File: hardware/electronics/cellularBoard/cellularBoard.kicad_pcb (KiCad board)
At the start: 4 copper layers, 22 x 36.8 mm, 56 parts, among them J1 Standoff, J2 M.2_E_Key_PCB_Edge, Q1 DMG1013TQ-7, U1 AP7361E, U2 TXS0104VxRUTR, U3 ZED-F9P, U4 OPA344

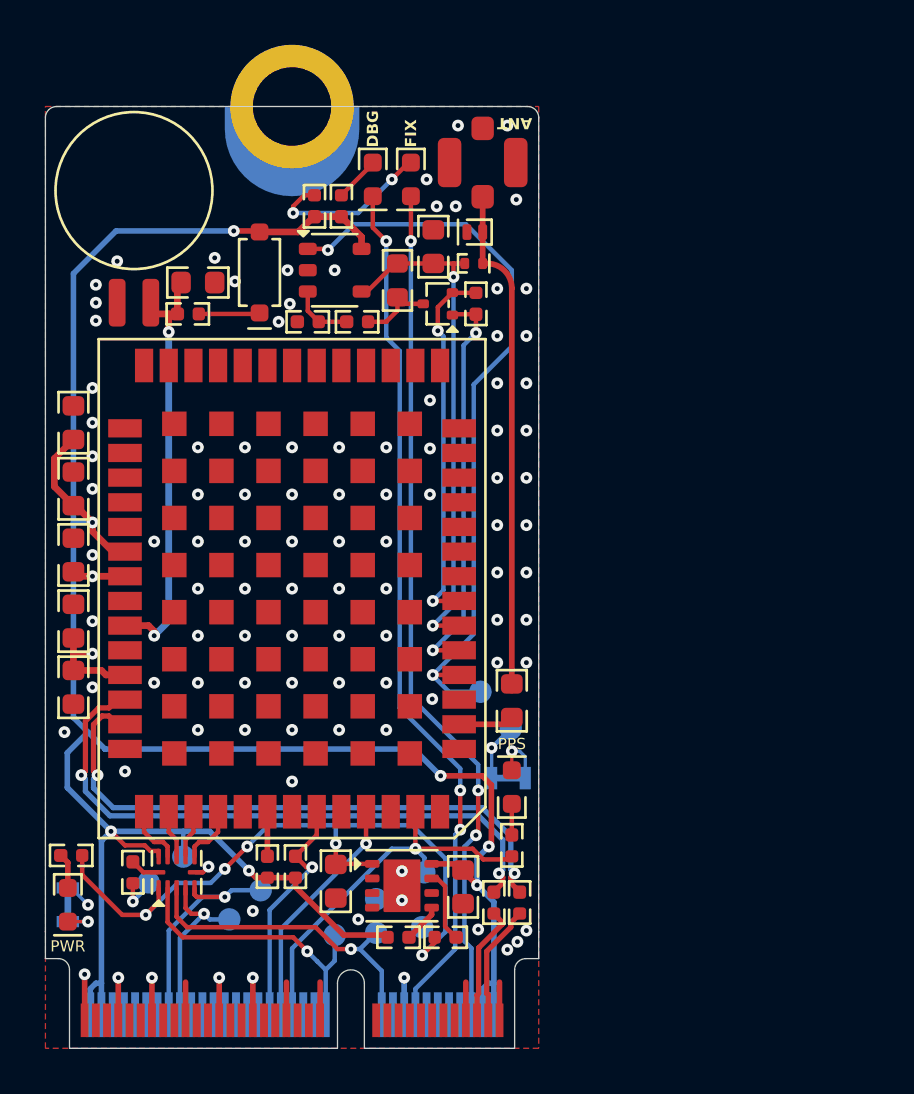
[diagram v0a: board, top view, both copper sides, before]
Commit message: first attempt for layout and routing
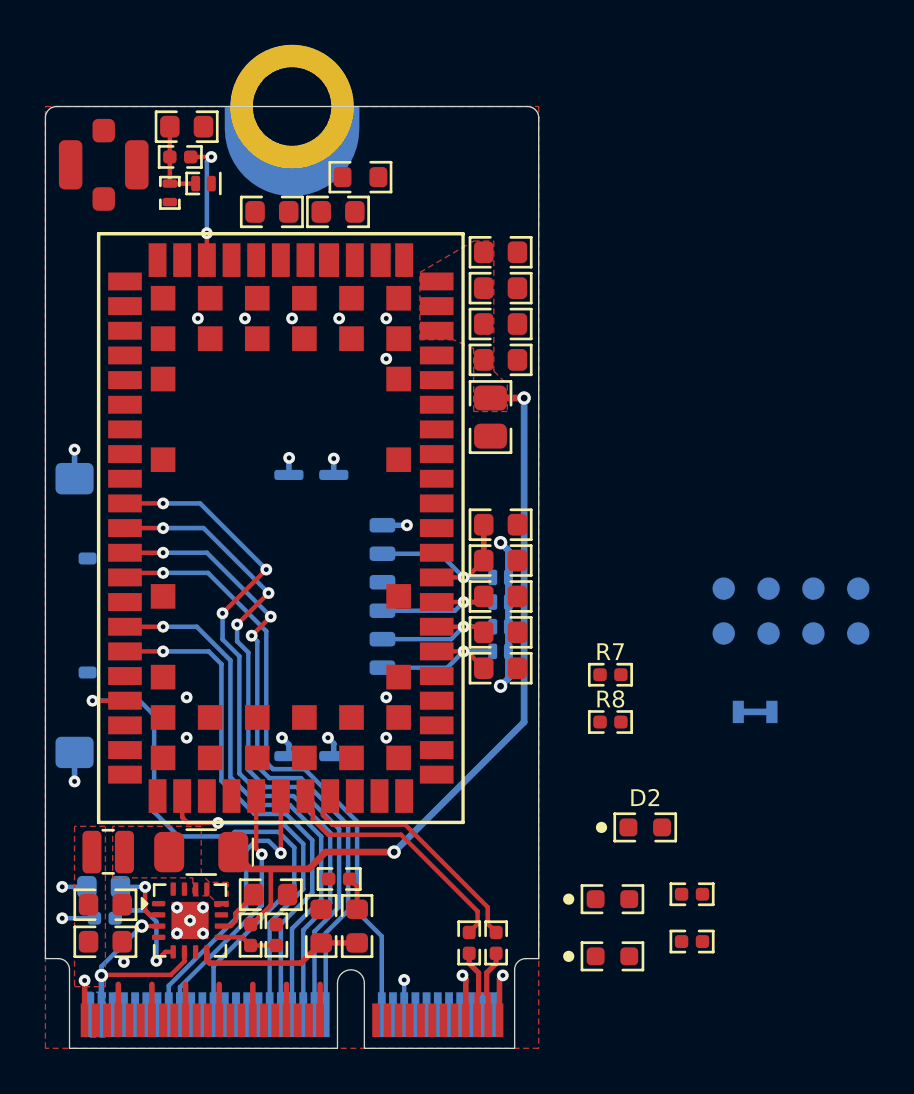
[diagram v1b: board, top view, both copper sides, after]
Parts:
- removed BT1: ~, lib_fp:MS621FE-FL11E
- removed JP2: ~, lib_fp:Jumper_2_Bridged
- removed Q1: DMG1013TQ-7, lib_fp:SOT23-3P50_160X160X75L22X22N
- removed R12: 27R, lib_fp:CRCW0402
- removed R13, R14: 10K, lib_fp:CRCW0402
- removed R15: 1K, lib_fp:CRCW0402
- removed R16: 100K, lib_fp:CRCW0402
- removed REF**: OSHW-Logo2_7.3x6mm_SilkScreen, DS-Logos-and-Graphics:OSHW-Logo2_7.3x6mm_SilkScreen
- removed TP10, TP11, TP9: ~, lib_fp:TP_1mm
- removed U3: ZED-F9P, lib_fp:ZED-F9P-04B_UBL
- removed U4: OPA344, lib_fp:SOT23-5P95_280X300X110L40X38N
- added C11: 15pF, lib_fp:MLCC0603, F.Cu at (149.3, 86.1)
- added C12: 47pF, lib_fp:MLCC0603, F.Cu at (149.3, 98.2)
- added C13: 100nF, lib_fp:MLCC0603, F.Cu at (149.3, 96.7)
- added C14: 47pF, lib_fp:MLCC0603, F.Cu at (149.3, 99.8)
- added C15: 47pF, lib_fp:MLCC0603, F.Cu at (149.3, 103.0)
- added C16: 47pF, lib_fp:MLCC0603, F.Cu at (149.3, 101.5)
- added C17: 15pF, lib_fp:MLCC0603, F.Cu at (142.1, 82.7)
- added C18: 33pF, lib_fp:MLCC0603, F.Cu at (139.1, 82.7)
- added C19: 27pF, lib_fp:MLCC0603, F.Cu at (135.3, 78.9)
- added D7: TVS, lib_fp:XDFN2P65_100X60X50L50X25L, B.Cu at (149.3, 102.3)
- added D8: TVS, lib_fp:XDFN2P65_100X60X50L50X25L, B.Cu at (149.3, 101.2)
- added D9: TVS, lib_fp:XDFN2P65_100X60X50L50X25L, F.Cu at (136.1, 81.4)
- added J3: 0786463001, lib_fp:786463001, B.Cu at (130.3, 100.7)
- added L2: 39nH, lib_fp:L_0603, F.Cu at (143.1, 81.2)
- added L3: 68nH, lib_fp:L_0402, F.Cu at (134.6, 81.8)
- C10: value 10nF -> 68pF
- C2, C8: value 2.2uF -> 100nF
- C3: moved to B.Cu
- C4: value 100nF -> 10nF
- C5: value 100nF -> 330pF
- C6: value 1uF -> 10nF
- C7: value 100nF -> 22uF; footprint lib_fp:MLCC0603 -> lib_fp:MLCC0805
- C9: value 47pF -> 10nF
- D1: value LTST-C190KYKT -> MBR230S1F; footprint lib_fp:LTST-0603 -> lib_fp:SOD123F
- D2: value LTST-C190KGKT -> LTST-C190KYKT
- D3: value LTST-C190KRKT -> LTST-C190KGKT
- D4: value LTST-C190TBKT -> LTST-C190KRKT
- D5: value B0540WQ -> TVS; footprint lib_fp:SOD123 -> lib_fp:XDFN2P65_100X60X50L50X25L; moved to B.Cu
- D6: value PTVS4V5D1BLYL -> TVS; footprint lib_fp:SOD882 -> lib_fp:XDFN2P65_100X60X50L50X25L; moved to B.Cu
- L1: value 47nH -> 680nH; footprint lib_fp:L_0402 -> lib_fp:L_0806
- R1: value 10K -> 9K31; moved to B.Cu
- R10: value 10R -> 27R; footprint lib_fp:CRCW0603 -> lib_fp:CRCW0402
- R11: value 27R -> 10K
- R2: value 10K -> 301R
- R3: value 1K -> 6K98
- R4: value 4K7 -> 2K49
- R6: value 10K -> 4K7
- R7: value 4K7 -> 10K
- R9: value 3K3 -> 27R
- U1: value AP7361E -> LM51571-Q1; footprint lib_fp:UDFN8P65_300X300X60L25X45L -> lib_fp:RTE0016K
- U2: value TXS0104VxRUTR -> SARA-R520-02B; footprint lib_fp:RUT0012A -> lib_fp:SARA-R52X_UBL
- moved R11 36.5 mm to (135.0, 80.2), turned to 180 degrees
- moved R5 34.4 mm to (157.8, 113.1), turned to 0 degrees
- moved D3 33.8 mm to (154.3, 113.3), turned to 0 degrees
- moved R4 32.5 mm to (139.3, 115.0), turned to 90 degrees
- moved TP1 32.4 mm to (165.2, 99.5)
- moved JP1 31.8 mm to (160.7, 105.0), turned to 180 degrees
- moved R9 31.2 mm to (149.1, 115.3), turned to 90 degrees
- moved L1 30.9 mm to (131.8, 111.2), turned to 0 degrees
- moved D2 30.7 mm to (155.8, 110.2), turned to 0 degrees
- moved R10 29.7 mm to (147.9, 115.3), turned to 90 degrees
- moved TP7 28.8 mm to (159.2, 99.5)
- moved TP5 28.2 mm to (161.2, 99.5)
- moved TP6 25.4 mm to (161.2, 101.5)
- moved TP4 25.2 mm to (163.2, 101.5)
- moved R6 25.1 mm to (157.8, 115.2), turned to 0 degrees
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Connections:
- AE1 pad 1: /Cellular Module/ANT_IN -> Net-(AE1-A)
- C10 pad 1: /Cellular Module/ANT_SHORT_N -> +3V8
- C2 pad 1: +1V8 -> +3V3
- C3 pad 1: +3V3 -> VSS
- C3 pad 2: VSS -> Net-(U1-VCC)
- C4 pad 1: +3V3 -> Net-(U1-SS)
- C5 pad 1: +3V3 -> Net-(U1-COMP)
- C6 pad 1: +3V3 -> Net-(U1-COMP)
- C6 pad 2: VSS -> Net-(C6-Pad2)
- C7 pad 1: +3V3 -> +3V8
- C8 pad 1: VBAT -> +3V8
- C9 pad 1: /Cellular Module/ANT_IN -> +3V8
- C9 pad 2: /Cellular Module/RF_IN -> VSS
- D1 pad 1: Net-(D1-Pad1) -> /SW
- D1 pad 2: Net-(D1-Pad2) -> +3V8
- D2 pad 1: Net-(D2-Pad1) -> +3V8
- D2 pad 2: Net-(J2-~{LED_1}) -> Net-(D2-Pad2)
- D3 pad 2: Net-(J2-~{LED_2}) -> Net-(J2-~{LED_1})
- D4 pad 2: Net-(D4-Pad2) -> Net-(J2-~{LED_2})
- D5 pad 1: +3V3 -> VSS
- D5 pad 2: Net-(D5-Pad2) -> VSIM
- D6 pad 2: /Cellular Module/ANT_IN -> /Cellular Modem/SIM_RST
- J2 pad 22: /ZED_RXD_1V8 -> /SARA_RXD_1V8
- J2 pad 32: /ZED_TXD_1V8 -> /SARA_TXD_1V8
- J2 pad 34: unconnected-(J2-UART_CTS-Pad34) -> /SARA_CTS_1V8
- J2 pad 36: unconnected-(J2-UART_RTS-Pad36) -> /SARA_RTS_1V8
- J2 pad 38: /PPS -> /SLEEP
- J2 pad 40: /EXTINT -> /NETWORK_STS
- J2 pad 42: /RESET_N -> /MODULE_STS
- J2 pad 52: unconnected-(J2-~{PERST0}-Pad52) -> /RESET_N
- J2 pad 56: /W_DISABLE -> unconnected-(J2-~{W_DISABLE1}-Pad56)
- J2 pad 58: /SDA_1V8 -> /SARA_SDA_1V8
- J2 pad 60: /SCL_1V8 -> /SARA_SCL_1V8
- JP1 pad 2: Net-(D1-Pad2) -> Net-(D2-Pad2)
- L1 pad 1: /Cellular Module/ANT_IN -> +3V3
- L1 pad 2: /Cellular Module/ANT_SHORT_N -> /SW
- R1 pad 1: +3V3 -> Net-(U1-RT)
- R1 pad 2: Net-(U1-EN) -> VSS
- R10 pad 1: /Cellular Module/ANT_SHORT_N -> /HOST_D-
- R10 pad 2: Net-(Q1-Pad3) -> /Cellular Modem/SARA_D-
- R11 pad 1: /HOST_D+ -> /Cellular Modem/ANT_DET
- R11 pad 2: /Cellular Module/ZED_D+ -> Net-(C19-Pad1)
- R2 pad 1: +1V8 -> Net-(C6-Pad2)
- R2 pad 2: Net-(U1-PG) -> VSS
- R3 pad 1: +1V8 -> +3V8
- R3 pad 2: Net-(D1-Pad1) -> Net-(U1-FB)
- R4 pad 1: Net-(D2-Pad1) -> Net-(U1-FB)
- R4 pad 2: +3V3 -> VSS
- R6 pad 1: VSS -> Net-(D4-Pad1)
- R6 pad 2: Net-(U2-OE) -> +3V3
- R7 pad 1: /PPS -> +1V8
- R7 pad 2: Net-(D4-Pad1) -> /SARA_SDA_1V8
- R8 pad 1: +3V3 -> +1V8
- R8 pad 2: /RESET_N -> /SARA_SCL_1V8
- R9 pad 1: Net-(D5-Pad2) -> /HOST_D+
- R9 pad 2: VBAT -> /Cellular Modem/SARA_D+
- TP3 pad 1: /ZED_RXD_1V8 -> /SARA_RXD_1V8
- TP4 pad 1: /ZED_TXD_1V8 -> /SARA_TXD_1V8
- TP5 pad 1: /SDA_1V8 -> /SARA_SDA_1V8
- TP6 pad 1: /SCL_1V8 -> /SARA_SCL_1V8
- U1 pad 1: +1V8 -> VSS
- U1 pad 2: unconnected-(U1-NC-Pad2) -> Net-(U1-VCC)
- U1 pad 3: unconnected-(U1-ADJ-Pad3) -> +3V3
- U1 pad 4: VSS -> unconnected-(U1-PGOOD-Pad4)
- U1 pad 5: Net-(U1-EN) -> Net-(U1-RT)
- U1 pad 6: unconnected-(U1-NC-Pad6) -> +3V3
- U1 pad 7: Net-(U1-PG) -> VSS
- U1 pad 8: +3V3 -> Net-(U1-COMP)
- U1 pad 9: VSS -> Net-(U1-FB)
- U2 pad 1: +1V8 -> VSS
- U2 pad 10: /Cellular Module/ZED_TXD_3V3 -> /SARA_RTS_1V8
- U2 pad 11: +3V3 -> /SARA_CTS_1V8
- U2 pad 12: Net-(U2-OE) -> /SARA_TXD_1V8
- U2 pad 2: /ZED_TXD_1V8 -> unconnected-(U2-RSVD-Pad2)
- U2 pad 3: /ZED_RXD_1V8 -> VSS
- U2 pad 4: /SDA_1V8 -> +1V8
- U2 pad 5: /SCL_1V8 -> VSS
- U2 pad 6: VSS -> unconnected-(U2-DSR-Pad6)
- U2 pad 7: /Cellular Module/SCL_3V3 -> unconnected-(U2-RI-Pad7)
- U2 pad 8: /Cellular Module/SDA_3V3 -> unconnected-(U2-DCD-Pad8)
- U2 pad 9: /Cellular Module/ZED_RXD_3V3 -> unconnected-(U2-DTR-Pad9)
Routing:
- net +3V3: track 120.5 -> 9.83 mm, vias 9 -> 2
- net Net-(J2-~{LED_2}): track 38.9 -> 0.00 mm, vias 3 -> 0
- net Net-(J2-~{LED_1}): track 38.4 -> 0.00 mm, vias 3 -> 0
- net +3V8: track 0.00 -> 34.8 mm, vias 0 -> 2
- net /Cellular Module/ANT_DET: track 33.6 -> 0.00 mm, vias 2 -> 0
- net +1V8: track 31.6 -> 0.00 mm, vias 5 -> 0
- net /SARA_RTS_1V8: track 0.00 -> 31.5 mm, vias 0 -> 3
- net /SARA_CTS_1V8: track 0.00 -> 30.1 mm, vias 0 -> 3
- net /SARA_TXD_1V8: track 0.00 -> 28.8 mm, vias 0 -> 3
- net /Cellular Module/ZED_D-: track 27.6 -> 0.00 mm, vias 2 -> 0
- net /SARA_RXD_1V8: track 0.00 -> 27.5 mm, vias 0 -> 1
- net /Cellular Module/ZED_D+: track 27.0 -> 0.00 mm, vias 2 -> 0
- net /SLEEP: track 0.00 -> 24.2 mm, vias 0 -> 1
- net /NETWORK_STS: track 0.00 -> 23.3 mm, vias 0 -> 1
- net /Cellular Module/ANT_SHORT_N: track 22.8 -> 0.00 mm, vias 2 -> 0
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- added copper zone on B.Cu, net +3V3
- added copper zone on F.Cu, net +3V3
- added copper zone on F.Cu, net +3V8
- added copper zone on F.Cu, net /SW
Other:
- board text removed: "ANT"
- board text removed: "DBG"
- board text removed: "FIX"
- board text removed: "PPS"
- board text removed: "PWR"

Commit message: cleaned up PCB
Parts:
- removed D8, D9: TVS, lib_fp:XDFN2P65_100X60X50L50X25L
- removed R10, R9: 27R, lib_fp:CRCW0402
- removed R11: 10K, lib_fp:CRCW0402
- C10: value 68pF -> 330pF
- C11: value 15pF -> 10nF
- C12: value 47pF -> 15pF; footprint lib_fp:MLCC0603 -> lib_fp:MLCC0402
- C13: value 100nF -> 33pF; footprint lib_fp:MLCC0603 -> lib_fp:MLCC0402
- C17: value 15pF -> 100nF
- C18: value 33pF -> 47pF
- C19: footprint lib_fp:MLCC0603 -> lib_fp:MLCC0402
- C3: value 1uF -> 22uF; footprint lib_fp:MLCC0603 -> lib_fp:MLCC0805; moved to F.Cu
- C4: value 10nF -> 100nF
- C5: value 330pF -> 10nF
- C6: value 10nF -> 68pF
- C7: value 22uF -> 15pF; footprint lib_fp:MLCC0805 -> lib_fp:MLCC0603
- C8: value 100nF -> 1uF; moved to B.Cu
- D3: value LTST-C190KGKT -> TVS; footprint lib_fp:LTST-0603 -> lib_fp:XDFN2P65_100X60X50L50X25L; moved to B.Cu
- D4: value LTST-C190KRKT -> TVS; footprint lib_fp:LTST-0603 -> lib_fp:XDFN2P65_100X60X50L50X25L; moved to B.Cu
- D7: moved to F.Cu
- J1: value Standoff -> M.2_E_Key_PCB_Edge; footprint lib_fp:M.2-Screw-Pad -> lib_fp:M.2 E-Key
- J2: value M.2_E_Key_PCB_Edge -> Standoff; footprint lib_fp:M.2 E-Key -> lib_fp:M.2-Screw-Pad
- L2: footprint lib_fp:L_0603 -> lib_fp:L_0402
- R1: value 9K31 -> 6K98; moved to F.Cu
- R2: value 301R -> 1K
- R3: value 6K98 -> 10K; moved to B.Cu
- R4: value 2K49 -> 10K; moved to B.Cu
- R5: value 4K7 -> 2K49
- R6: value 4K7 -> 9K31; moved to B.Cu
- R7: value 10K -> 301R
- TP1: value ~ -> +3V8
- TP2, TP8: value ~ -> VSS
- TP3: value ~ -> SCL
- TP4: value ~ -> SDA
- TP5: value ~ -> RXD
- TP6: value ~ -> TXD
- TP7: value ~ -> +1V8
- moved J1 42.0 mm to (140.0, 120.0)
- moved J2 42.0 mm to (140.0, 78.0)
- moved TP2 33.2 mm to (133.0, 109.5)
- moved TP7 31.7 mm to (129.8, 111.1)
- moved TP4 31.0 mm to (134.2, 112.2)
- moved C9 30.4 mm to (139.1, 113.2)
- moved TP5 30.2 mm to (131.8, 92.6)
- moved TP8 29.8 mm to (131.8, 90.0)
- moved TP3 29.7 mm to (137.1, 113.5)
- moved C8 29.4 mm to (131.7, 112.8)
- moved C11 29.2 mm to (142.9, 114.5), turned to 90 degrees
- moved C6 29.2 mm to (149.3, 86.1), turned to 0 degrees
- moved R8 28.6 mm to (136.7, 82.8)
- moved TP6 28.4 mm to (134.3, 92.6)
- moved C10 28.0 mm to (141.3, 114.5), turned to 90 degrees
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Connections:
- AE1 pad 1: Net-(AE1-A) -> /ANT_IN
- C10 pad 1: +3V8 -> Net-(U1-COMP)
- C11 pad 1: +3V8 -> Net-(U1-COMP)
- C11 pad 2: VSS -> Net-(C11-Pad2)
- C12 pad 1: VSIM -> /RF_IN
- C12 pad 2: VSS -> Net-(C12-Pad2)
- C13 pad 1: VSIM -> Net-(C12-Pad2)
- C13 pad 2: VSS -> /ANT_IN
- C14 pad 1: /Cellular Modem/SIM_RST -> /SIM_IO
- C15 pad 1: /Cellular Modem/SIM_CLK -> /SIM_CLK
- C16 pad 1: /Cellular Modem/SIM_IO -> /SIM_RST
- C17 pad 1: /Cellular Modem/RF_IN -> VSIM
- C17 pad 2: Net-(C17-Pad2) -> VSS
- C18 pad 1: Net-(C17-Pad2) -> VSIM
- C18 pad 2: Net-(AE1-A) -> VSS
- C3 pad 1: VSS -> +3V8
- C3 pad 2: Net-(U1-VCC) -> VSS
- C4 pad 1: Net-(U1-SS) -> +3V8
- C5 pad 1: Net-(U1-COMP) -> +3V8
- C6 pad 1: Net-(U1-COMP) -> +3V8
- C6 pad 2: Net-(C6-Pad2) -> VSS
- C8 pad 1: +3V8 -> VSS
- C8 pad 2: VSS -> Net-(U1-VCC)
- C9 pad 1: +3V8 -> Net-(U1-SS)
- D2 pad 1: +3V8 -> Net-(D2-Pad1)
- D3 pad 1: Net-(D3-Pad1) -> VSS
- D3 pad 2: Net-(J2-~{LED_1}) -> /SIM_IO
- D4 pad 1: Net-(D4-Pad1) -> VSS
- D4 pad 2: Net-(J2-~{LED_2}) -> /SIM_CLK
- D5 pad 2: VSIM -> /SIM_RST
- D6 pad 2: /Cellular Modem/SIM_RST -> VSIM
- D7 pad 2: /Cellular Modem/SIM_CLK -> Net-(C19-Pad1)
- J3 pad C2: /Cellular Modem/SIM_RST -> /SIM_RST
- J3 pad C3: /Cellular Modem/SIM_CLK -> /SIM_CLK
- J3 pad C7: /Cellular Modem/SIM_IO -> /SIM_IO
- L2 pad 1: Net-(C17-Pad2) -> Net-(C12-Pad2)
- L3 pad 1: Net-(AE1-A) -> /ANT_IN
- R1 pad 1: Net-(U1-RT) -> +3V8
- R1 pad 2: VSS -> Net-(U1-FB)
- R2 pad 1: Net-(C6-Pad2) -> +3V8
- R2 pad 2: VSS -> Net-(D2-Pad1)
- R3 pad 1: +3V8 -> +1V8
- R3 pad 2: Net-(U1-FB) -> /SARA_SDA_1V8
- R4 pad 1: Net-(U1-FB) -> +1V8
- R4 pad 2: VSS -> /SARA_SCL_1V8
- R5 pad 1: Net-(D3-Pad1) -> Net-(U1-FB)
- R5 pad 2: +3V3 -> VSS
- R6 pad 1: Net-(D4-Pad1) -> Net-(U1-RT)
- R6 pad 2: +3V3 -> VSS
- R7 pad 1: +1V8 -> Net-(C11-Pad2)
- R7 pad 2: /SARA_SDA_1V8 -> VSS
- R8 pad 1: +1V8 -> /ANT_DET
- R8 pad 2: /SARA_SCL_1V8 -> Net-(C19-Pad1)
- TP1 pad 1: +3V3 -> +3V8
- TP2 pad 1: +1V8 -> VSS
- TP3 pad 1: /SARA_RXD_1V8 -> /SARA_SCL_1V8
- TP4 pad 1: /SARA_TXD_1V8 -> /SARA_SDA_1V8
- TP5 pad 1: /SARA_SDA_1V8 -> /SARA_RXD_1V8
- TP6 pad 1: /SARA_SCL_1V8 -> /SARA_TXD_1V8
- TP7 pad 1: VSS -> +1V8
- U2 pad 19: /Cellular Modem/PPS -> unconnected-(U2-GPIO6-Pad19)
- U2 pad 28: /Cellular Modem/SARA_D- -> unconnected-(U2-USB_D--Pad28)
- U2 pad 29: /Cellular Modem/SARA_D+ -> unconnected-(U2-USB_D+-Pad29)
- U2 pad 38: /Cellular Modem/SIM_CLK -> /SIM_CLK
- U2 pad 39: /Cellular Modem/SIM_IO -> /SIM_IO
- U2 pad 40: /Cellular Modem/SIM_RST -> /SIM_RST
- U2 pad 56: /Cellular Modem/RF_IN -> /RF_IN
- U2 pad 62: /Cellular Modem/ANT_DET -> /ANT_DET
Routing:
- net +1V8: track 0.00 -> 30.2 mm, vias 0 -> 1
- net +3V3: track 9.83 -> 29.6 mm, vias 2 -> 3
- net /Cellular Modem/SARA_D-: track 11.3 -> 0.00 mm
- net /Cellular Modem/SARA_D+: track 11.3 -> 0.00 mm
- net /SARA_SDA_1V8: track 11.4 -> 21.1 mm, vias 1 -> 3
- net /SIM_CLK: track 0.00 -> 7.63 mm, vias 0 -> 1
- net /Cellular Modem/SIM_CLK: track 7.63 -> 0.00 mm, vias 1 -> 0
- net /SIM_IO: track 0.00 -> 7.35 mm, vias 0 -> 1
- net /Cellular Modem/SIM_IO: track 7.35 -> 0.00 mm, vias 1 -> 0
- net /SIM_RST: track 0.00 -> 7.28 mm, vias 0 -> 1
- net /Cellular Modem/SIM_RST: track 7.28 -> 0.00 mm, vias 1 -> 0
- net Net-(C19-Pad1): track 3.69 -> 10.9 mm
- net /SARA_RXD_1V8: track 27.5 -> 34.7 mm
- net /SARA_TXD_1V8: track 28.8 -> 34.8 mm
- net /Cellular Modem/ANT_DET: track 5.60 -> 0.00 mm, vias 2 -> 0
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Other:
- board text added: "2x 20°±5°"
- board text added: "Board thickness is 0.8mm 4-Layer Beveled Edge ENIG Finish w/ Hard Gold Fingers"
- board text added: "Card Edge Bevel"
- board text added: "Embry-Riddle Aeronautical University Physical Sciences Department Madison Gleydura Master's Thesis 2024-12-21"
- board text added: "Fabrication Instructions"
- board text added: "LTE-M"
- board text added: "PWR"
- board text added: "SARA-R512 Cellular Modem"
- board text removed: "ZED-F9P GNSS M.2 E-Key Card Embry-Riddle Aeronautical University Physical Sciences Department Madison Gleydura Master's Thesis 2024-12-02"

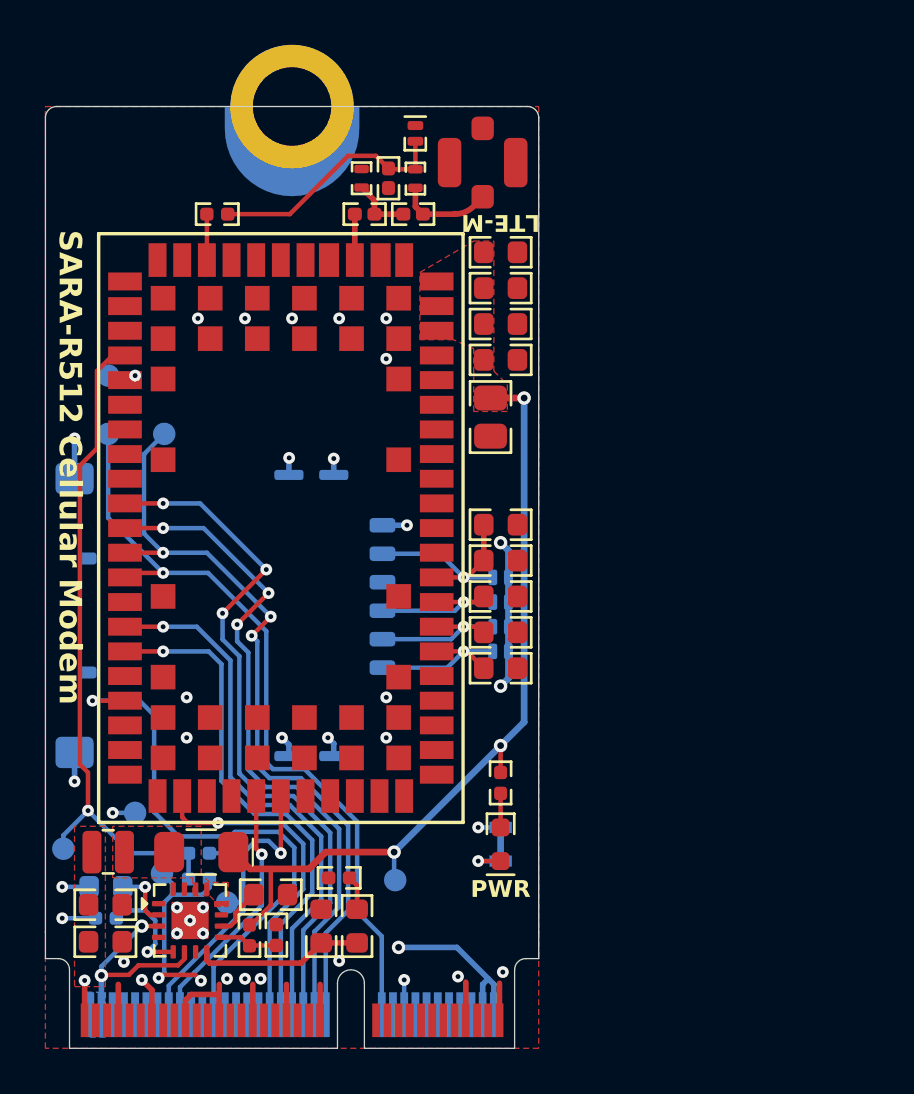
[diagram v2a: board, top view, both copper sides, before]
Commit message: cleaned up board and added fiducials
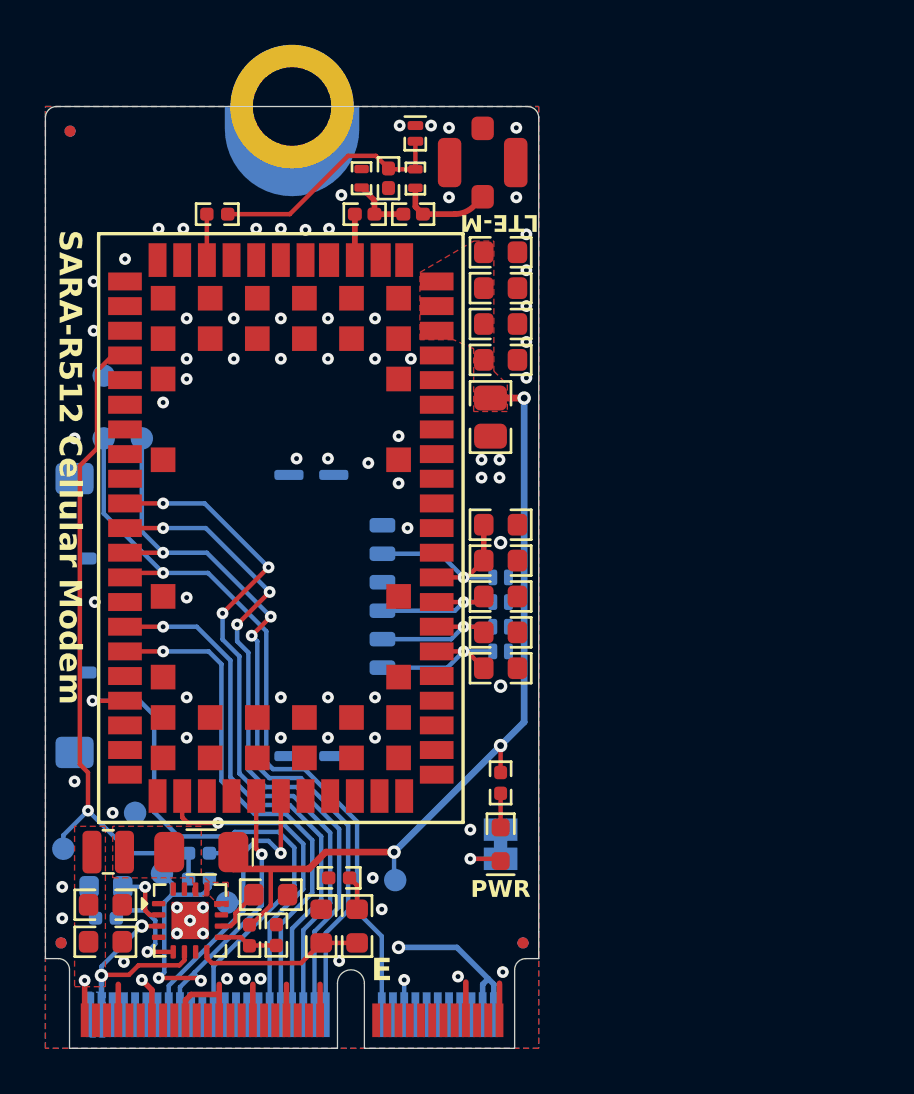
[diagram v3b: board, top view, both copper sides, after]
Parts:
- added REF**: Fiducial_0.5mm_Mask1mm, lib_fp:Fiducial_0.5mm_Mask1mm, F.Cu at (150.3, 115.3)
- added REF**: Fiducial_0.5mm_Mask1mm, lib_fp:Fiducial_0.5mm_Mask1mm, F.Cu at (129.7, 115.3)
- added REF**: Fiducial_0.5mm_Mask1mm, lib_fp:Fiducial_0.5mm_Mask1mm, F.Cu at (130.1, 79.1)
- added REF**: Fiducial_0.5mm_Mask1mm, lib_fp:Fiducial_0.5mm_Mask1mm, B.Cu at (150.3, 115.3)
- added REF**: Fiducial_0.5mm_Mask1mm, lib_fp:Fiducial_0.5mm_Mask1mm, B.Cu at (130.1, 79.1)
- added REF**: Fiducial_0.5mm_Mask1mm, lib_fp:Fiducial_0.5mm_Mask1mm, B.Cu at (129.7, 115.3)
- JP1: footprint lib_fp:Jumper_2_Bridged -> lib_fp:SolderJumper-2_P1.3mm_Bridged_Pad1.0x1.5mm
- moved TP6 1.02 mm to (133.3, 92.8)
- moved TP5 0.28 mm to (131.6, 92.8)
- moved TP8 0.20 mm to (131.6, 90.0)
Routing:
- net VSS: track 39.2 -> 19.2 mm, vias 39 -> 79
- net Net-(D2-Pad2): track 2.00 -> 2.74 mm
- added copper zone on B.Cu, net VSS
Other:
- board text added: "E"
- board text added: "Embry-Riddle Aeronautical University Physical Sciences Department"
- board text added: "Madison Gleydura Master's Thesis 2024-12-21"
- board text removed: "Embry-Riddle Aeronautical University Physical Sciences Department Madison Gleydura Master's Thesis 2024-12-21"
